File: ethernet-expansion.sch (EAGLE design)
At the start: 21 parts, among them Q1 25MHz, U1 ENC28J60-SO

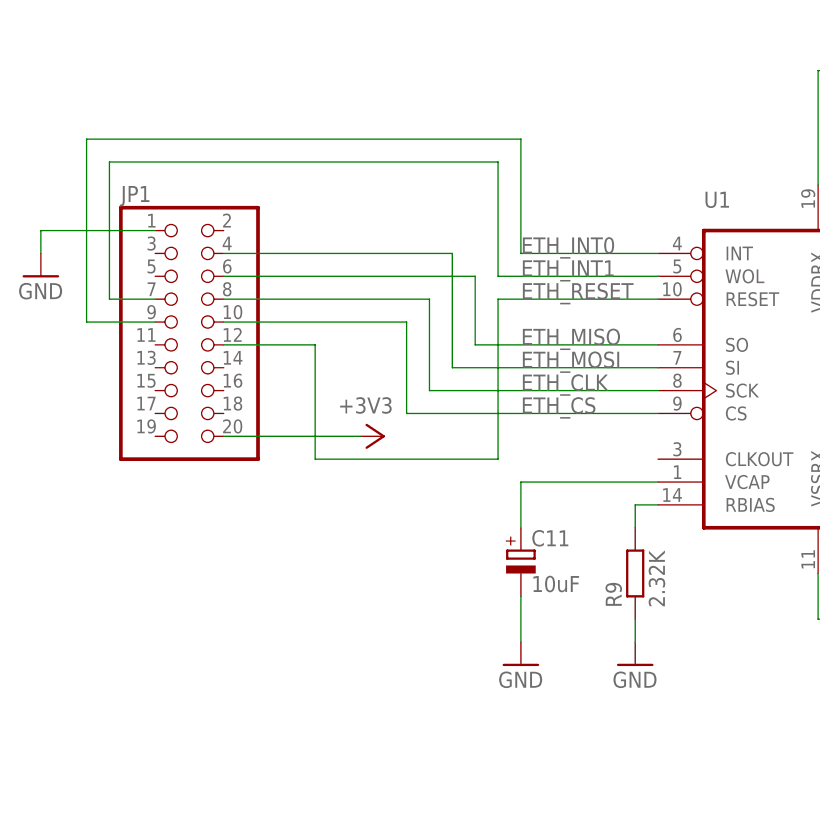
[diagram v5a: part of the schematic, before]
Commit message: Swapping header pin rows to make it correct, and adding debug uart pins
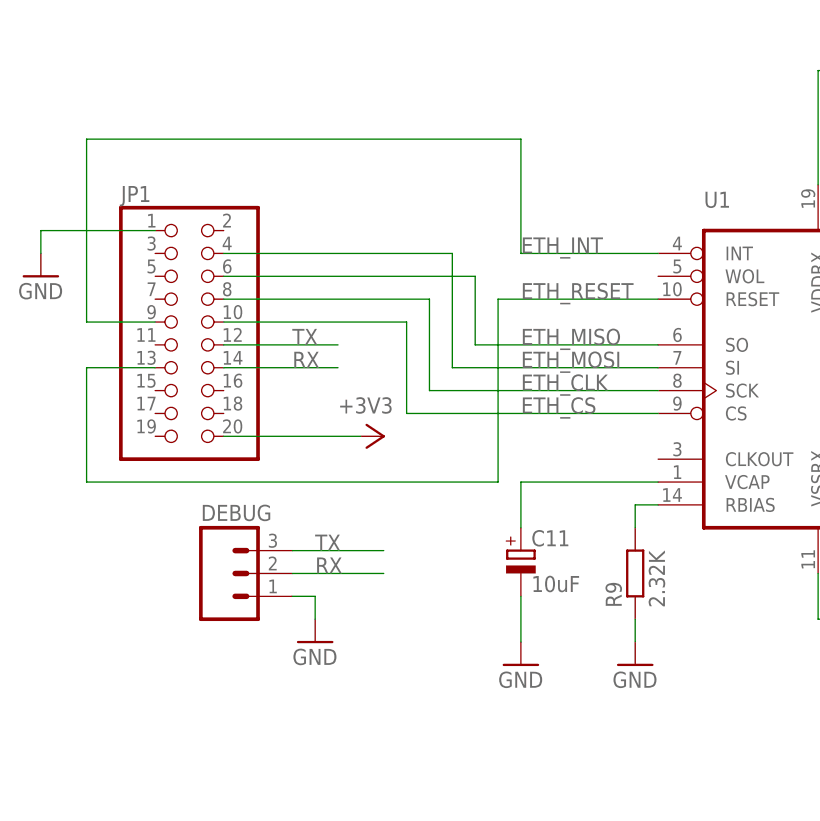
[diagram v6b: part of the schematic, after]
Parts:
- added DEBUG: (no value), SparkFun-Connectors:M03PTH
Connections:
- net ETH_INT0 renamed ETH_INT
- removed net ETH_INT1: JP1.7, U1.WOL
- new net RX: DEBUG.2, JP1.14
- new net TX: DEBUG.3, JP1.12
- net ETH_RESET: now also JP1.13; no longer JP1.12
- net GND: now also DEBUG.1
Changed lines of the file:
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@@
 <grid distance="0.1" unitdist="inch" unit="inch" style="lines" multiple="1" display="no" altdistance="0.01" altunitdist="inch" altunit="inch"/>
 <layers>
-<layer number="1" name="Top" color="4" fill="1" visible="yes" active="no"/>
-<layer number="16" name="Bottom" color="1" fill="1" visible="yes" active="no"/>
-<layer number="17" name="Pads" color="2" fill="1" visible="yes" active="no"/>
-<layer number="18" name="Vias" color="2" fill="1" visible="yes" active="no"/>
-<layer number="19" name="Unrouted" color="6" fill="1" visible="yes" active="no"/>
-<layer number="20" name="Dimension" color="15" fill="1" visible="yes" active="no"/>
-<layer number="21" name="tPlace" color="7" fill="1" visible="yes" active="no"/>
-<layer number="22" name="bPlace" color="7" fill="1" visible="yes" active="no"/>
-<layer number="23" name="tOrigins" color="15" fill="1" visible="yes" active="no"/>
-<layer number="24" name="bOrigins" color="15" fill="1" visible="yes" active="no"/>
-<layer number="25" name="tNames" color="7" fill="1" visible="yes" active="no"/>
-<layer number="26" name="bNames" color="7" fill="1" visible="yes" active="no"/>
-<layer number="27" name="tValues" color="7" fill="1" visible="yes" active="no"/>
-<layer number="28" name="bValues" color="7" fill="1" visible="yes" active="no"/>
+<layer number="1" name="Top" color="4" fill="1" visible="no" active="no"/>
+<layer number="16" name="Bottom" color="1" fill="1" visible="no" active="no"/>
+<layer number="17" name="Pads" color="2" fill="1" visible="no" active="no"/>
+<layer number="18" name="Vias" color="2" fill="1" visible="no" active="no"/>
+<layer number="19" name="Unrouted" color="6" fill="1" visible="no" active="no"/>
+<layer number="20" name="Dimension" color="15" fill="1" visible="no" active="no"/>
+<layer number="21" name="tPlace" color="7" fill="1" visible="no" active="no"/>
+<layer number="22" name="bPlace" color="7" fill="1" visible="no" active="no"/>
+<layer number="23" name="tOrigins" color="15" fill="1" visible="no" active="no"/>
+<layer number="24" name="bOrigins" color="15" fill="1" visible="no" active="no"/>
+<layer number="25" name="tNames" color="7" fill="1" visible="no" active="no"/>
+<layer number="26" name="bNames" color="7" fill="1" visible="no" active="no"/>
+<layer number="27" name="tValues" color="7" fill="1" visible="no" active="no"/>
+<layer number="28" name="bValues" color="7" fill="1" visible="no" active="no"/>
 <layer number="29" name="tStop" color="7" fill="3" visible="no" active="no"/>
 <layer number="30" name="bStop" color="7" fill="6" visible="no" active="no"/>
@@
 <layer number="35" name="tGlue" color="7" fill="4" visible="no" active="no"/>
 <layer number="36" name="bGlue" color="7" fill="5" visible="no" active="no"/>
-<layer number="37" name="tTest" color="7" fill="1" visible="yes" active="no"/>
-<layer number="38" name="bTest" color="7" fill="1" visible="yes" active="no"/>
+<layer number="37" name="tTest" color="7" fill="1" visible="no" active="no"/>
+<layer number="38" name="bTest" color="7" fill="1" visible="no" active="no"/>
 <layer number="39" name="tKeepout" color="4" fill="11" visible="no" active="no"/>
 <layer number="40" name="bKeepout" color="1" fill="11" visible="no" active="no"/>
@@
 <layer number="44" name="Drills" color="7" fill="1" visible="no" active="no"/>
 <layer number="45" name="Holes" color="7" fill="1" visible="no" active="no"/>
-<layer number="46" name="Milling" color="3" fill="1" visible="yes" active="no"/>
-<layer number="47" name="Measures" color="7" fill="1" visible="yes" active="no"/>
-<layer number="48" name="Document" color="7" fill="1" visible="yes" active="no"/>
-<layer number="49" name="Reference" color="7" fill="1" visible="yes" active="no"/>
-<layer number="50" name="dxf" color="7" fill="1" visible="yes" active="no"/>
-<layer number="51" name="tDocu" color="7" fill="1" visible="yes" active="no"/>
-<layer number="52" name="bDocu" color="7" fill="1" visible="yes" active="no"/>
-<layer number="53" name="tGND_GNDA" color="7" fill="9" visible="yes" active="no"/>
-<layer number="54" name="bGND_GNDA" color="1" fill="9" visible="yes" active="no"/>
-<layer number="56" name="wert" color="7" fill="1" visible="yes" active="no"/>
-<layer number="57" name="tCAD" color="7" fill="1" visible="yes" active="no"/>
-<layer number="59" name="tCarbon" color="7" fill="1" visible="yes" active="no"/>
-<layer number="60" name="bCarbon" color="7" fill="1" visible="yes" active="no"/>
+<layer number="46" name="Milling" color="3" fill="1" visible="no" active="no"/>
+<layer number="47" name="Measures" color="7" fill="1" visible="no" active="no"/>
+<layer number="48" name="Document" color="7" fill="1" visible="no" active="no"/>
+<layer number="49" name="Reference" color="7" fill="1" visible="no" active="no"/>
+<layer number="50" name="dxf" color="7" fill="1" visible="no" active="no"/>
+<layer number="51" name="tDocu" color="7" fill="1" visible="no" active="no"/>
+<layer number="52" name="bDocu" color="7" fill="1" visible="no" active="no"/>
+<layer number="53" name="tGND_GNDA" color="7" fill="9" visible="no" active="no"/>
+<layer number="54" name="bGND_GNDA" color="1" fill="9" visible="no" active="no"/>
+<layer number="56" name="wert" color="7" fill="1" visible="no" active="no"/>
+<layer number="57" name="tCAD" color="7" fill="1" visible="no" active="no"/>
+<layer number="59" name="tCarbon" color="7" fill="1" visible="no" active="no"/>
+<layer number="60" name="bCarbon" color="7" fill="1" visible="no" active="no"/>
 <layer number="90" name="Modules" color="5" fill="1" visible="yes" active="yes"/>
 <layer number="91" name="Nets" color="2" fill="1" visible="yes" active="yes"/>
@@
 <part name="GND15" library="supply1" deviceset="GND" device=""/>
 <part name="C11" library="resistor" deviceset="CPOL-EU" device="E2-4" value="10uF"/>
+<part name="DEBUG" library="SparkFun-Connectors" deviceset="M03" device="PTH"/>
+<part name="GND16" library="supply1" deviceset="GND" device=""/>
 </parts>
 <sheets>
@@
 <instance part="GND15" gate="1" x="119.38" y="73.66"/>
 <instance part="C11" gate="G$1" x="-12.7" y="45.72"/>
+<instance part="DEBUG" gate="G$1" x="-45.72" y="43.18"/>
+<instance part="GND16" gate="1" x="-35.56" y="35.56"/>
 </instances>
 <busses>
@@
 <wire x1="-66.04" y1="81.28" x2="-66.04" y2="78.74" width="0.1524" layer="91"/>
 </segment>
+<segment>
+<pinref part="DEBUG" gate="G$1" pin="1"/>
+<pinref part="GND16" gate="1" pin="GND"/>
+<wire x1="-38.1" y1="40.64" x2="-35.56" y2="40.64" width="0.1524" layer="91"/>
+<wire x1="-35.56" y1="40.64" x2="-35.56" y2="38.1" width="0.1524" layer="91"/>
+</segment>
 </net>
 <net name="N$8" class="0">
@@
 </segment>
 </net>
-<net name="ETH_INT0" class="0">
+<net name="ETH_INT" class="0">
 <segment>
 <pinref part="U1" gate="G$1" pin="INT"/>
@@
 <pinref part="U1" gate="G$1" pin="RESET"/>
 <wire x1="2.54" y1="73.66" x2="-15.24" y2="73.66" width="0.1524" layer="91"/>
-<wire x1="-15.24" y1="73.66" x2="-15.24" y2="55.88" width="0.1524" layer="91"/>
-<wire x1="-15.24" y1="55.88" x2="-35.56" y2="55.88" width="0.1524" layer="91"/>
-<wire x1="-35.56" y1="55.88" x2="-35.56" y2="68.58" width="0.1524" layer="91"/>
-<pinref part="JP1" gate="A" pin="12"/>
-<wire x1="-35.56" y1="68.58" x2="-45.72" y2="68.58" width="0.1524" layer="91"/>
+<wire x1="-15.24" y1="73.66" x2="-15.24" y2="53.34" width="0.1524" layer="91"/>
+<wire x1="-15.24" y1="53.34" x2="-60.96" y2="53.34" width="0.1524" layer="91"/>
 <label x="-12.7" y="73.66" size="1.778" layer="95"/>
+<wire x1="-60.96" y1="53.34" x2="-60.96" y2="66.04" width="0.1524" layer="91"/>
+<pinref part="JP1" gate="A" pin="13"/>
+<wire x1="-60.96" y1="66.04" x2="-53.34" y2="66.04" width="0.1524" layer="91"/>
 </segment>
 </net>
@@
 <wire x1="-12.7" y1="53.34" x2="-12.7" y2="48.26" width="0.1524" layer="91"/>
 <pinref part="C11" gate="G$1" pin="+"/>
-</segment>
-</net>
-<net name="ETH_INT1" class="0">
-<segment>
-<pinref part="U1" gate="G$1" pin="WOL"/>
-<wire x1="2.54" y1="76.2" x2="-15.24" y2="76.2" width="0.1524" layer="91"/>
-<label x="-12.7" y="76.2" size="1.778" layer="95"/>
-<wire x1="-15.24" y1="76.2" x2="-15.24" y2="88.9" width="0.1524" layer="91"/>
-<pinref part="JP1" gate="A" pin="7"/>
-<wire x1="-53.34" y1="73.66" x2="-58.42" y2="73.66" width="0.1524" layer="91"/>
-<wire x1="-15.24" y1="88.9" x2="-58.42" y2="88.9" width="0.1524" layer="91"/>
-<wire x1="-58.42" y1="88.9" x2="-58.42" y2="73.66" width="0.1524" layer="91"/>
 </segment>
 </net>
@@
 </segment>
 </net>
+<net name="TX" class="0">
+<segment>
+<pinref part="DEBUG" gate="G$1" pin="3"/>
+<wire x1="-38.1" y1="45.72" x2="-27.94" y2="45.72" width="0.1524" layer="91"/>
+<label x="-35.56" y="45.72" size="1.778" layer="95"/>
+</segment>
+<segment>
+<pinref part="JP1" gate="A" pin="12"/>
+<wire x1="-45.72" y1="68.58" x2="-33.02" y2="68.58" width="0.1524" layer="91"/>
+<label x="-38.1" y="68.58" size="1.778" layer="95"/>
+</segment>
+</net>
+<net name="RX" class="0">
+<segment>
+<pinref part="DEBUG" gate="G$1" pin="2"/>
+<wire x1="-38.1" y1="43.18" x2="-27.94" y2="43.18" width="0.1524" layer="91"/>
+<label x="-35.56" y="43.18" size="1.778" layer="95"/>
+</segment>
+<segment>
+<pinref part="JP1" gate="A" pin="14"/>
+<wire x1="-45.72" y1="66.04" x2="-33.02" y2="66.04" width="0.1524" layer="91"/>
+<label x="-38.1" y="66.04" size="1.778" layer="95"/>
+</segment>
+</net>
